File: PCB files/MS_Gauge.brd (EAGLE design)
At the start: 40 x 40 mm, 27 parts, among them IC1 B1836M, IC2 LPC11C24_QFP48, U1 MCP1700, U2 TSR1-2450, Y1 12MHz

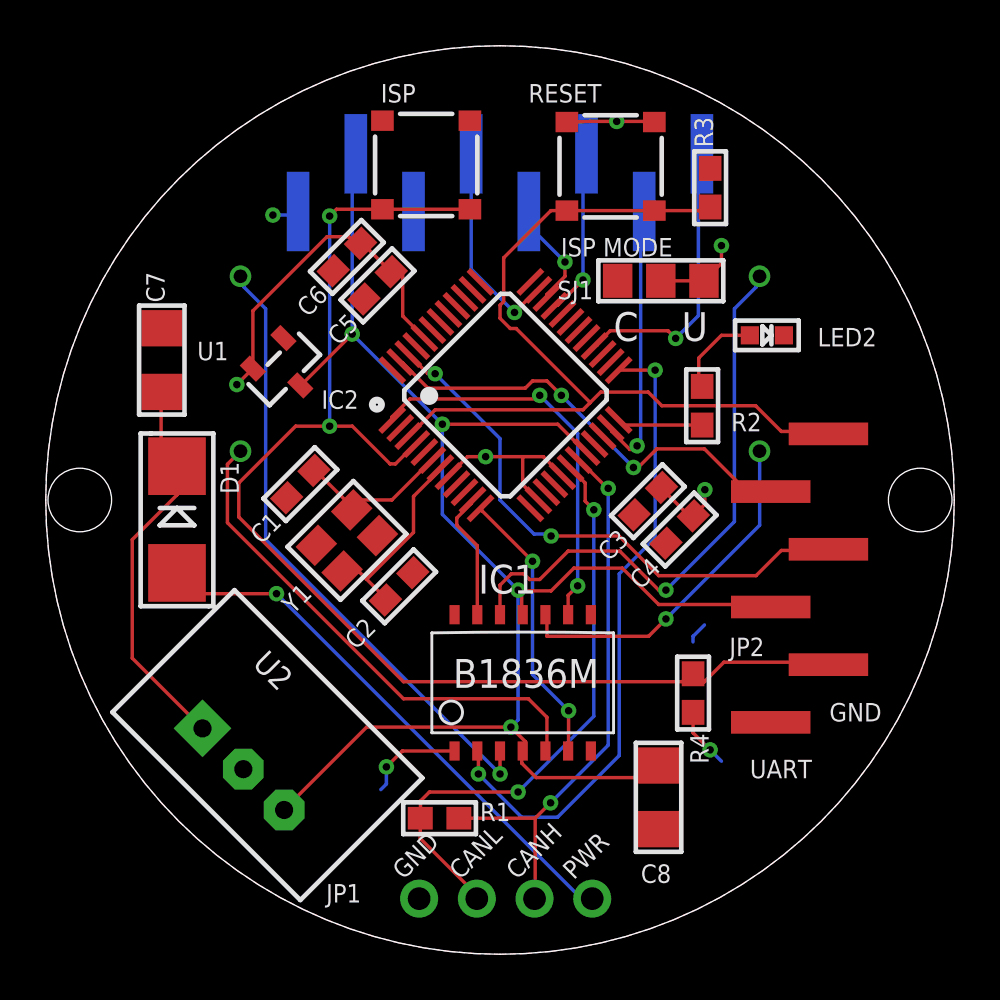
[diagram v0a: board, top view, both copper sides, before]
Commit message: Update Eagle files to Rev 4. Fixes wrong reset button wiring, adds termination resistor solder jumper.
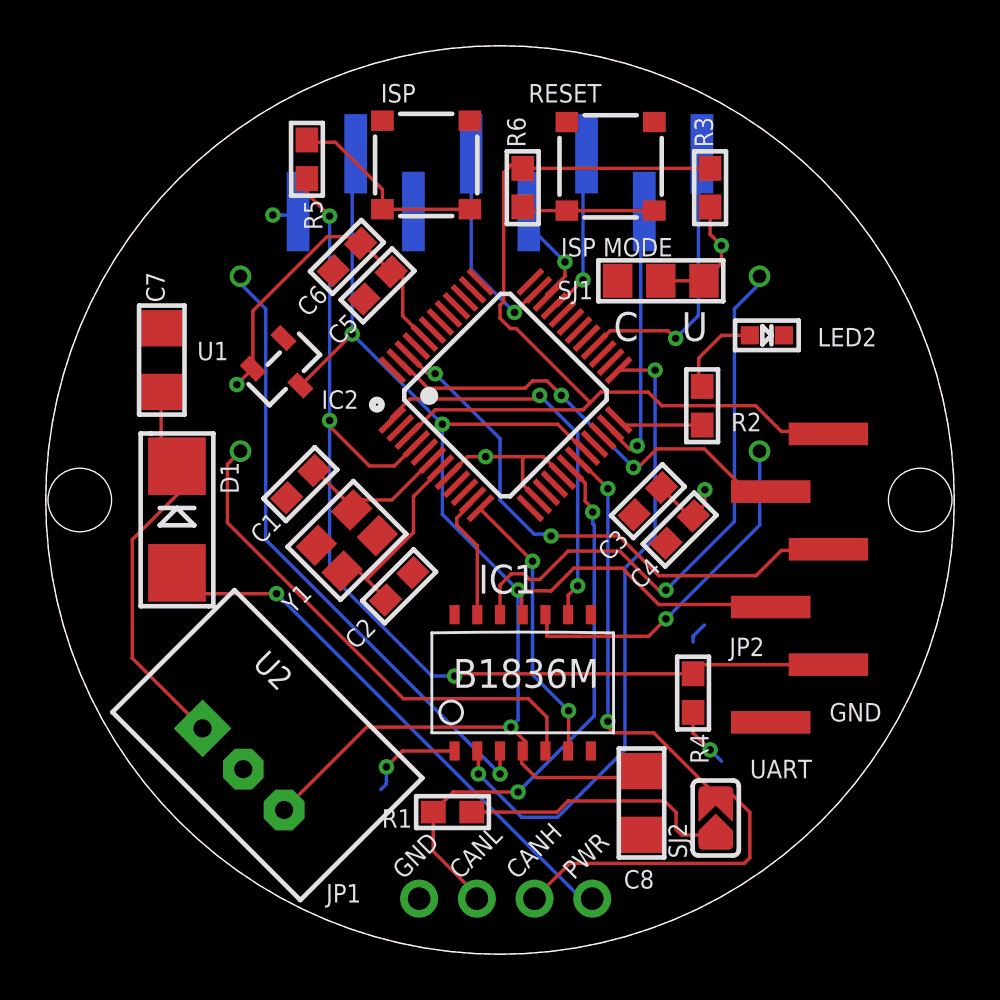
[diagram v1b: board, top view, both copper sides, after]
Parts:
- added R5, R6: 33, microbuilder:0603
- added SJ2: (no value), microbuilder:SOLDERJUMPER_ARROW_NOPASTE
- moved C8 0.79 mm to (26.2, 6.66)
- moved R1 0.63 mm to (17.9, 6.26), turned to 180 degrees
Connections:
- new net N$17: IC2.19, JP1.3, SJ2.2
- new net N$6: IC2.4, JP2.2, R4.1, R5.2
- new net N$8: B1.B, B1.D, R6.1
- net 3.3V: now also R3.1; no longer B1.A, B1.C
- net GND: now also B1.A, B1.C; no longer R3.2
- net N$1: now also R1.1, SJ2.1; no longer IC2.19, JP1.3, R1.2
- net N$13: now also R3.2, R6.2; no longer B1.B, B1.D, R3.1
- net N$2: now also R1.2; no longer R1.1
- net N$5: now also R5.1; no longer IC2.4, JP2.2, R4.1
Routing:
- net N$5: track 56.9 -> 8.95 mm, vias 2 -> 0
- net N$6: track 0.00 -> 47.0 mm, vias 0 -> 3
- net N$17: track 0.00 -> 32.3 mm, vias 0 -> 2
- net N$1: track 24.8 -> 12.1 mm, vias 2 -> 0
- net N$8: track 0.00 -> 5.86 mm
- net N$13: track 38.4 -> 41.4 mm
- net 3.3V: track 42.5 -> 40.6 mm, vias 7 -> 6
- net N$2: track 26.1 -> 25.0 mm
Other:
- board text added: "MS Gauge Rev 4"
- board text removed: "MS Gauge Rev 3"

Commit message: Update Eagle files to Rev 5. Adds i2c eeprom.
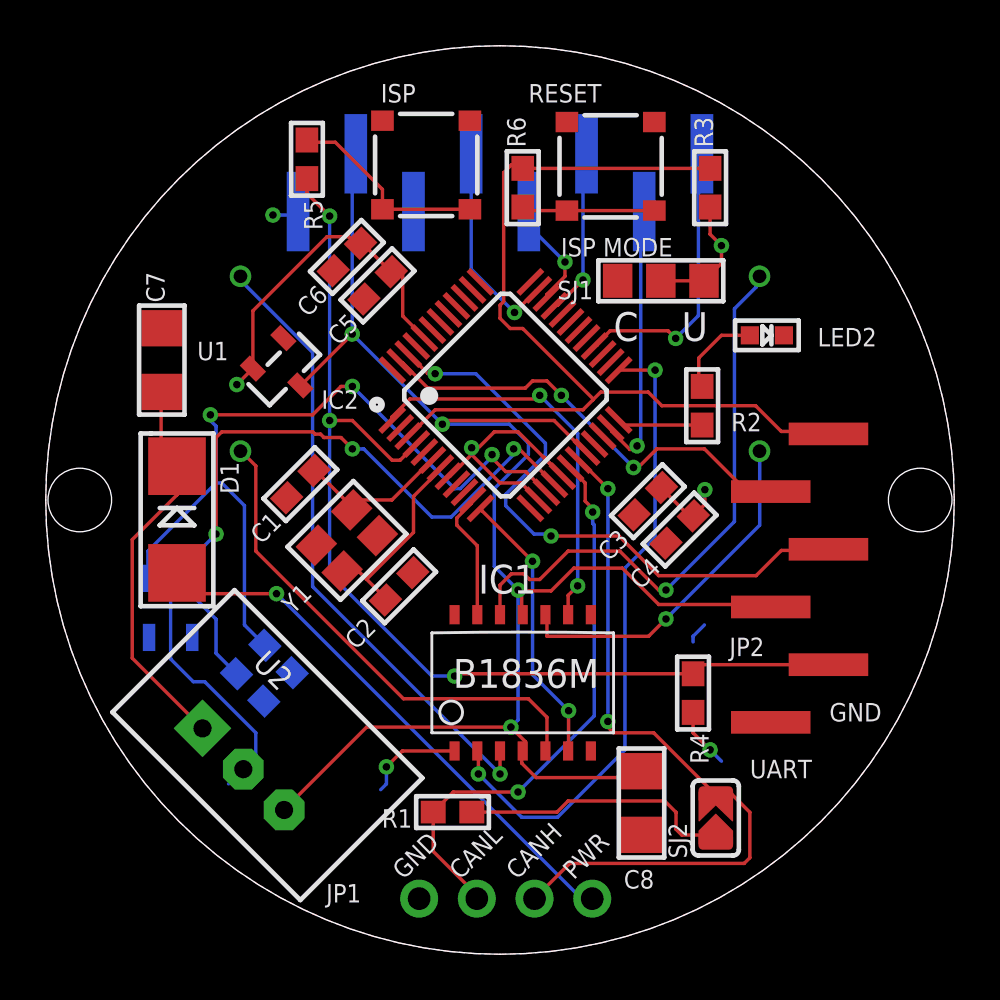
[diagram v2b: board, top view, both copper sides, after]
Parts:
- added IC3: 24LC32AT-I/OT, microchip:SOT23-5L
- added R7, R8: 2k, microbuilder:0603
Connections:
- new net SCL: IC2.15, IC3.1, R8.1
- new net SDA: IC2.16, IC3.3, R7.1
- net 3.3V: now also IC3.4, R7.2, R8.2
- net GND: now also IC3.2
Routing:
- net SCL: track 0.00 -> 35.4 mm, vias 0 -> 3
- net SDA: track 0.00 -> 30.4 mm, vias 0 -> 3
- net GND: track 1.17 -> 12.6 mm
- net 3.3V: track 40.6 -> 44.6 mm
- net 5.0V: track 72.3 -> 75.5 mm
- net N$18: track 24.6 -> 27.1 mm
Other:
- board text added: "MS Gauge Rev 5"
- board text removed: "MS Gauge Rev 4"

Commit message: Minor routing changes to PCB
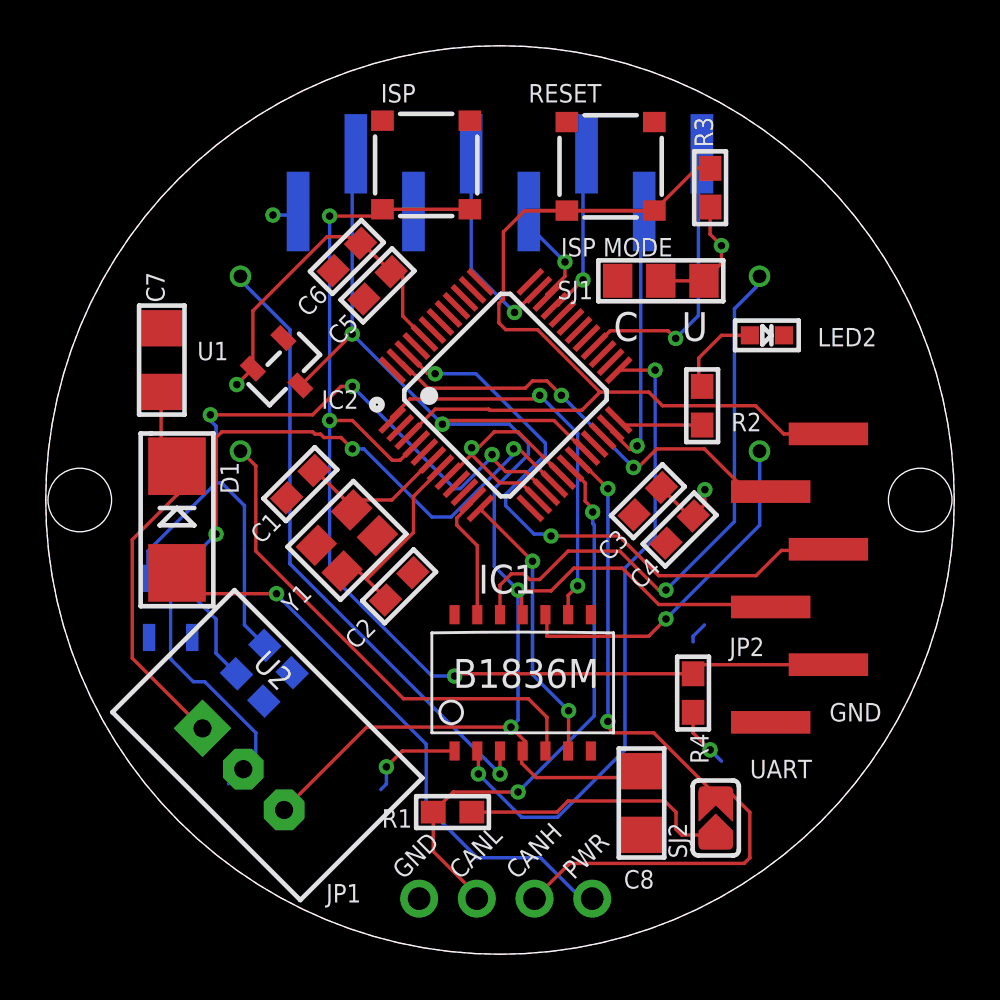
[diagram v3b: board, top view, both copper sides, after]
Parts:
- removed R5, R6: 33, microbuilder:0603
- R2: value 2k -> 120
- R7, R8: value 2k -> 4.7k
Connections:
- removed net N$13: IC2.3, JP2.6, R3.2, R6.2
- removed net N$5: B2.A, B2.C, R5.1
- net N$6: now also B2.A, B2.C; no longer R5.2
- net N$8: now also IC2.3, JP2.6, R3.2; no longer R6.1
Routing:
- net N$13: track 41.5 -> 0.00 mm
- net N$8: track 5.86 -> 45.8 mm
- net N$5: track 8.95 -> 0.00 mm
- net N$6: track 46.9 -> 51.2 mm
- net 12V: track 24.2 -> 25.9 mm
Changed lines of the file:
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@@
 <attribute name="VALUE" x="30.48" y="25.98" size="0.4064" layer="27" ratio="10"/>
 </element>
-<element name="R2" library="microbuilder" package="0603" value="2k" x="28.9" y="24.15" smashed="yes" rot="R270">
+<element name="R2" library="microbuilder" package="0603" value="120" x="28.9" y="24.15" smashed="yes" rot="R270">
 <attribute name="NAME" x="30.178" y="23.023" size="0.8128" layer="25" font="vector" ratio="18"/>
 <attribute name="VALUE" x="28.138" y="22.372" size="0.4064" layer="27" font="vector" ratio="10" rot="R270"/>
@@
 <attribute name="VALUE" x="20.306" y="32.464" size="0.4064" layer="27" ratio="10" rot="R90"/>
 </element>
-<element name="R5" library="microbuilder" package="0603" value="33" x="11.5" y="35" rot="R270"/>
-<element name="R6" library="microbuilder" package="0603" value="33" x="21" y="33.75" rot="R90"/>
 <element name="SJ2" library="microbuilder" package="SOLDERJUMPER_ARROW_NOPASTE" value="" x="29.5" y="6" rot="R90">
 <attribute name="BOM" value="EXCLUDE" x="29.5" y="6" size="1.778" layer="27" rot="R90" display="off"/>
 </element>
-<element name="R7" library="microbuilder" package="0603" value="2k" x="9" y="11.75" rot="MR225"/>
-<element name="R8" library="microbuilder" package="0603" value="2k" x="10.25" y="13" rot="MR225"/>
+<element name="R7" library="microbuilder" package="0603" value="4.7k" x="9" y="11.75" rot="MR225"/>
+<element name="R8" library="microbuilder" package="0603" value="4.7k" x="10.25" y="13" rot="MR225"/>
 <element name="IC3" library="microchip" package="SOT23-5L" value="24LC32AT-I/OT" x="5.5" y="15.25" rot="MR180"/>
 </elements>
@@
 <wire x1="6.6675" y1="15.875" x2="5.87375" y2="16.66875" width="0.1524" layer="1"/>
 <wire x1="10.16" y1="15.875" x2="6.6675" y2="15.875" width="0.1524" layer="1"/>
-<wire x1="23.495" y1="2.54" x2="10.16" y2="15.875" width="0.1524" layer="16"/>
 <wire x1="23.97125" y1="2.54" x2="23.495" y2="2.54" width="0.1524" layer="16"/>
 <wire x1="5.87375" y1="16.66875" x2="5.78" y2="16.7905" width="0.1524" layer="1"/>
 <wire x1="23.97125" y1="2.54" x2="24.06" y2="2.45" width="0.1524" layer="16"/>
 <via x="10.16" y="15.875" extent="1-16" drill="0.3302"/>
+<wire x1="23.495" y1="2.54" x2="21.785" y2="4.25" width="0.1524" layer="16"/>
+<wire x1="21.785" y1="4.25" x2="19" y2="4.25" width="0.1524" layer="16"/>
+<wire x1="19" y1="4.25" x2="16.75" y2="6.5" width="0.1524" layer="16"/>
+<wire x1="16.75" y1="6.5" x2="16.75" y2="9.25" width="0.1524" layer="16"/>
+<wire x1="16.75" y1="9.25" x2="10.16" y2="15.84" width="0.1524" layer="16"/>
+<wire x1="10.16" y1="15.84" x2="10.16" y2="15.875" width="0.1524" layer="16"/>
 </signal>
 <signal name="N$12">
@@
 <wire x1="31.79" y1="20.5" x2="31.92" y2="20.37" width="0.1524" layer="1"/>
 </signal>
-<signal name="N$13">
-<contactref element="IC2" pad="3"/>
-<contactref element="JP2" pad="6"/>
-<wire x1="17.145" y1="23.97125" x2="16.03375" y2="22.86" width="0.1524" layer="1"/>
-<wire x1="23.65375" y1="23.97125" x2="17.145" y2="23.97125" width="0.1524" layer="1"/>
-<wire x1="24.4325" y1="24.75" x2="24.09125" y2="24.40875" width="0.1524" layer="1"/>
-<wire x1="24.09125" y1="24.40875" x2="23.65375" y2="23.97125" width="0.1524" layer="1"/>
-<wire x1="32.385" y1="23.01875" x2="31.25375" y2="24.15" width="0.1524" layer="1"/>
-<wire x1="34.44875" y1="23.01875" x2="32.385" y2="23.01875" width="0.1524" layer="1"/>
-<wire x1="16.03375" y1="22.86" x2="15.962003125" y2="22.816875" width="0.1524" layer="1"/>
-<wire x1="34.44875" y1="23.01875" x2="34.46" y2="22.91" width="0.1524" layer="1"/>
-<wire x1="20.0025" y1="28.575" x2="20.16125" y2="28.73375" width="0.1524" layer="1"/>
-<wire x1="26.52625" y1="24.75" x2="27.12625" y2="24.15" width="0.1524" layer="1"/>
-<wire x1="27.12625" y1="24.15" x2="31.25375" y2="24.15" width="0.1524" layer="1"/>
-<wire x1="24.4325" y1="24.75" x2="26.52625" y2="24.75" width="0.1524" layer="1"/>
-<wire x1="20.0025" y1="28.575" x2="20.0025" y2="27.9975" width="0.1524" layer="1"/>
-<wire x1="20.0025" y1="27.9975" x2="20.45" y2="27.55" width="0.1524" layer="1"/>
-<contactref element="R3" pad="2"/>
-<contactref element="R6" pad="2"/>
-<wire x1="20.16125" y1="28.73375" x2="20.16125" y2="34.41125" width="0.1524" layer="1"/>
-<wire x1="20.16125" y1="34.41125" x2="20.5" y2="34.75" width="0.1524" layer="1"/>
-<wire x1="20.5" y1="34.75" x2="20.85" y2="34.75" width="0.1524" layer="1"/>
-<wire x1="20.85" y1="34.75" x2="21" y2="34.6" width="0.1524" layer="1"/>
-<wire x1="21" y1="34.6" x2="29.25" y2="34.6" width="0.1524" layer="1"/>
-<wire x1="20.45" y1="27.55" x2="21" y2="27.55" width="0.1524" layer="1"/>
-<wire x1="21" y1="27.55" x2="24.09125" y2="24.45875" width="0.1524" layer="1"/>
-<wire x1="24.09125" y1="24.45875" x2="24.09125" y2="24.40875" width="0.1524" layer="1"/>
-</signal>
 <signal name="N$23">
 <contactref element="U$18" pad="CLK"/>
@@
 <wire x1="8.73125" y1="29.845" x2="8.575" y2="29.85" width="0.1524" layer="16"/>
 <via x="20.0025" y="7.9375" extent="1-16" drill="0.3302"/>
-<wire x1="20.0025" y1="7.9375" x2="11.75" y2="16.19" width="0.1524" layer="16"/>
-<wire x1="11.75" y1="16.19" x2="11.75" y2="26.5" width="0.1524" layer="16"/>
-<wire x1="11.75" y1="26.5" x2="8.575" y2="29.675" width="0.1524" layer="16"/>
+<wire x1="20.0025" y1="7.9375" x2="10.75" y2="17.19" width="0.1524" layer="16"/>
+<wire x1="10.75" y1="17.19" x2="10.75" y2="27.5" width="0.1524" layer="16"/>
+<wire x1="10.75" y1="27.5" x2="8.575" y2="29.675" width="0.1524" layer="16"/>
 <wire x1="8.575" y1="29.675" x2="8.575" y2="29.85" width="0.1524" layer="16"/>
 </signal>
@@
 <contactref element="IC2" pad="4"/>
 <contactref element="R4" pad="1"/>
-<contactref element="R5" pad="2"/>
-<wire x1="11.5" y1="34.15" x2="11.5" y2="33.5" width="0.1524" layer="1"/>
-<wire x1="11.5" y1="33.5" x2="12.5" y2="32.5" width="0.1524" layer="1"/>
 <via x="12.5" y="32.5" extent="1-16" drill="0.3302"/>
 <wire x1="12.5" y1="32.5" x2="12.5" y2="23.5" width="0.1524" layer="16"/>
@@
 <wire x1="15.25" y1="21.75" x2="13.5" y2="23.5" width="0.1524" layer="1"/>
 <wire x1="13.5" y1="23.5" x2="12.5" y2="23.5" width="0.1524" layer="1"/>
-</signal>
-<signal name="N$5">
 <contactref element="B2" pad="C"/>
 <contactref element="B2" pad="A"/>
-<contactref element="R5" pad="1"/>
-<wire x1="14.825" y1="32.8" x2="18.675" y2="32.8" width="0.1524" layer="1"/>
-<wire x1="14.825" y1="32.8" x2="14.825" y2="33.675" width="0.1524" layer="1"/>
-<wire x1="14.825" y1="33.675" x2="12.75" y2="35.75" width="0.1524" layer="1"/>
-<wire x1="12.75" y1="35.75" x2="11.6" y2="35.75" width="0.1524" layer="1"/>
-<wire x1="11.6" y1="35.75" x2="11.5" y2="35.85" width="0.1524" layer="1"/>
+<wire x1="18.675" y1="32.8" x2="14.825" y2="32.8" width="0.1524" layer="1"/>
+<wire x1="14.825" y1="32.8" x2="14.525" y2="32.5" width="0.1524" layer="1"/>
+<wire x1="14.525" y1="32.5" x2="12.5" y2="32.5" width="0.1524" layer="1"/>
 </signal>
 <signal name="N$8">
 <contactref element="B1" pad="D"/>
 <contactref element="B1" pad="B"/>
-<contactref element="R6" pad="1"/>
 <wire x1="22.945" y1="32.74" x2="26.795" y2="32.74" width="0.1524" layer="1"/>
 <wire x1="22.945" y1="32.74" x2="21.16" y2="32.74" width="0.1524" layer="1"/>
-<wire x1="21.16" y1="32.74" x2="21" y2="32.9" width="0.1524" layer="1"/>
+<contactref element="R3" pad="2"/>
+<contactref element="IC2" pad="3"/>
+<contactref element="JP2" pad="6"/>
+<wire x1="29.25" y1="34.6" x2="28.655" y2="34.6" width="0.1524" layer="1"/>
+<wire x1="28.655" y1="34.6" x2="26.795" y2="32.74" width="0.1524" layer="1"/>
+<wire x1="34.46" y1="22.91" x2="32.49" y2="22.91" width="0.1524" layer="1"/>
+<wire x1="32.49" y1="22.91" x2="31.25" y2="24.15" width="0.1524" layer="1"/>
+<wire x1="31.25" y1="24.15" x2="27.15" y2="24.15" width="0.1524" layer="1"/>
+<wire x1="27.15" y1="24.15" x2="26.55" y2="24.75" width="0.1524" layer="1"/>
+<wire x1="26.55" y1="24.75" x2="24.4" y2="24.75" width="0.1524" layer="1"/>
+<wire x1="24.4" y1="24.75" x2="23.6" y2="23.95" width="0.1524" layer="1"/>
+<wire x1="26.795" y1="32.74" x2="21.09" y2="32.74" width="0.1524" layer="1"/>
+<wire x1="21.09" y1="32.74" x2="20.15" y2="31.8" width="0.1524" layer="1"/>
+<wire x1="20.15" y1="31.8" x2="20.15" y2="28.85" width="0.1524" layer="1"/>
+<wire x1="20.15" y1="28.85" x2="19.95" y2="28.65" width="0.1524" layer="1"/>
+<wire x1="19.95" y1="28.65" x2="19.95" y2="27.8" width="0.1524" layer="1"/>
+<wire x1="19.95" y1="27.8" x2="20.25" y2="27.5" width="0.1524" layer="1"/>
+<wire x1="20.25" y1="27.5" x2="21.65" y2="27.5" width="0.1524" layer="1"/>
+<wire x1="21.65" y1="27.5" x2="24.4" y2="24.75" width="0.1524" layer="1"/>
+<wire x1="23.6" y1="23.95" x2="19.55" y2="23.95" width="0.1524" layer="1"/>
+<wire x1="19.55" y1="23.95" x2="19.5" y2="24" width="0.1524" layer="1"/>
+<wire x1="19.5" y1="24" x2="17.15" y2="24" width="0.1524" layer="1"/>
+<wire x1="17.15" y1="24" x2="15.966875" y2="22.816875" width="0.1524" layer="1"/>
+<wire x1="15.966875" y1="22.816875" x2="15.962003125" y2="22.816875" width="0.1524" layer="1"/>
 </signal>
 <signal name="N$17">
